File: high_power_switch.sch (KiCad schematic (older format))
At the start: 3 parts, among them Q5 Q_NMOS_DGS, U6 BTS6133D

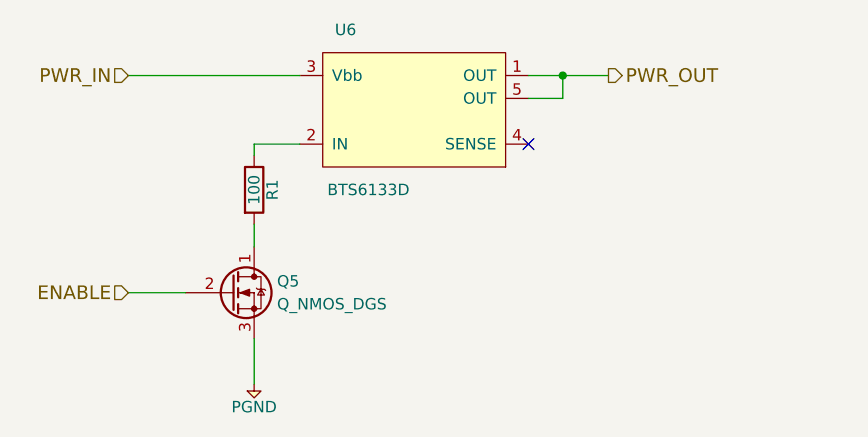
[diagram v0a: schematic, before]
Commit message: add LEDs to indicate switch condition; fix hierarchical sheet issues
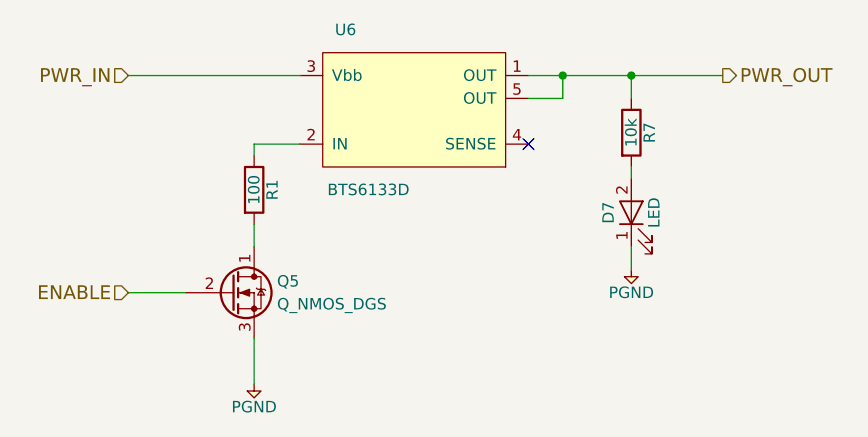
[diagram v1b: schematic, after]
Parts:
- added D7: LED, symbol LED
- added R7: 10k, symbol R
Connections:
- net PGND: now also D7.1 (K)
- net PWR_OUT: now also R7.1
- new net: D7.2 (A), R7.2
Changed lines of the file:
@@
 	6450 3450 6450 3350
 Wire Wire Line
-	6300 3350 6650 3350
+	6300 3350 7150 3350
 Connection ~ 6450 3350
-Text HLabel 6650 3350 2    60   Output ~ 0
+Text HLabel 7150 3350 2    60   Output ~ 0
 PWR_OUT
 NoConn ~ 6300 3650
@@
 P 5100 4700
 AR Path="/5957D255/596222E8/5962B512" Ref="#PWR?"  Part="1"
-AR Path="/5957D255/596398D9/5962B512" Ref="#PWR16"  Part="1"
-F 0 "#PWR16" H 4970 4740 50  0001 L CNN
+AR Path="/5957D255/596398D9/5962B512" Ref="#PWR021"  Part="1"
+F 0 "#PWR021" H 4970 4740 50  0001 L CNN
 F 1 "PGND" H 5100 4600 50  0000 C CNN
 F 2 "" H 5100 4700 60  0001 C CNN
@@
 	1    0    0    -1
 $EndComp
+$Comp
+L R R7
+U 1 1 596A68DB
+P 6750 3600
+F 0 "R7" V 6830 3600 50  0000 C CNN
+F 1 "10k" V 6750 3600 50  0000 C CNN
+F 2 "" V 6680 3600 50  0001 C CNN
+F 3 "" H 6750 3600 50  0001 C CNN
+	1    6750 3600
+	1    0    0    -1
+$EndComp
+Wire Wire Line
+	6750 3450 6750 3350
+Connection ~ 6750 3350
+$Comp
+L LED D7
+U 1 1 596A6916
+P 6750 3950
+F 0 "D7" H 6750 4050 50  0000 C CNN
+F 1 "LED" H 6750 3850 50  0000 C CNN
+F 2 "" H 6750 3950 50  0001 C CNN
+F 3 "" H 6750 3950 50  0001 C CNN
+	1    6750 3950
+	0    -1   -1   0
+$EndComp
+Wire Wire Line
+	6750 3800 6750 3750
+$Comp
+L PGND #PWR022
+U 1 1 596A695D
+P 6750 4200
+F 0 "#PWR022" H 6620 4240 50  0001 L CNN
+F 1 "PGND" H 6750 4100 50  0000 C CNN
+F 2 "" H 6750 4200 60  0001 C CNN
+F 3 "" H 6750 4200 60  0001 C CNN
+	1    6750 4200
+	1    0    0    -1
+$EndComp
+Wire Wire Line
+	6750 4100 6750 4200
 $EndSCHEMATC

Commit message: assign footprints to components
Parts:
- D7: footprint (none) -> LEDs:LED_0805
- Q5: footprint (none) -> TO_SOT_Packages_SMD:SOT-669_LFPAK
- R1, R7: footprint (none) -> Resistors_SMD:R_0603
- U6: footprint (none) -> TO_SOT_Packages_SMD:TO-252-5_TabPin3
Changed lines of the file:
@@
 F 0 "Q5" H 5200 4350 50  0000 L CNN
 F 1 "Q_NMOS_DGS" H 5200 4250 50  0000 L CNN
-F 2 "" H 5200 4400 50  0001 C CNN
+F 2 "TO_SOT_Packages_SMD:SOT-669_LFPAK" H 5200 4400 50  0001 C CNN
 F 3 "" H 5000 4300 50  0001 C CNN
 	1    5000 4300
@@
 F 0 "R1" V 5180 3850 50  0000 C CNN
 F 1 "100" V 5100 3850 50  0000 C CNN
-F 2 "" V 5030 3850 50  0001 C CNN
+F 2 "Resistors_SMD:R_0603" V 5030 3850 50  0001 C CNN
 F 3 "" H 5100 3850 50  0001 C CNN
 	1    5100 3850
@@
 F 0 "U6" H 5500 3750 50  0000 C CNN
 F 1 "BTS6133D" H 5600 3050 50  0000 C CNN
-F 2 "" H 6850 3050 50  0001 C CNN
+F 2 "TO_SOT_Packages_SMD:TO-252-5_TabPin3" H 6850 3050 50  0001 C CNN
 F 3 "" H 6850 3050 50  0001 C CNN
 	1    5800 3450
@@
 F 0 "R7" V 6830 3600 50  0000 C CNN
 F 1 "10k" V 6750 3600 50  0000 C CNN
-F 2 "" V 6680 3600 50  0001 C CNN
+F 2 "Resistors_SMD:R_0603" V 6680 3600 50  0001 C CNN
 F 3 "" H 6750 3600 50  0001 C CNN
 	1    6750 3600
@@
 F 0 "D7" H 6750 4050 50  0000 C CNN
 F 1 "LED" H 6750 3850 50  0000 C CNN
-F 2 "" H 6750 3950 50  0001 C CNN
+F 2 "LEDs:LED_0805" H 6750 3950 50  0001 C CNN
 F 3 "" H 6750 3950 50  0001 C CNN
 	1    6750 3950
